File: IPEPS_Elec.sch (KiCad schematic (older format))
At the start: 6 parts

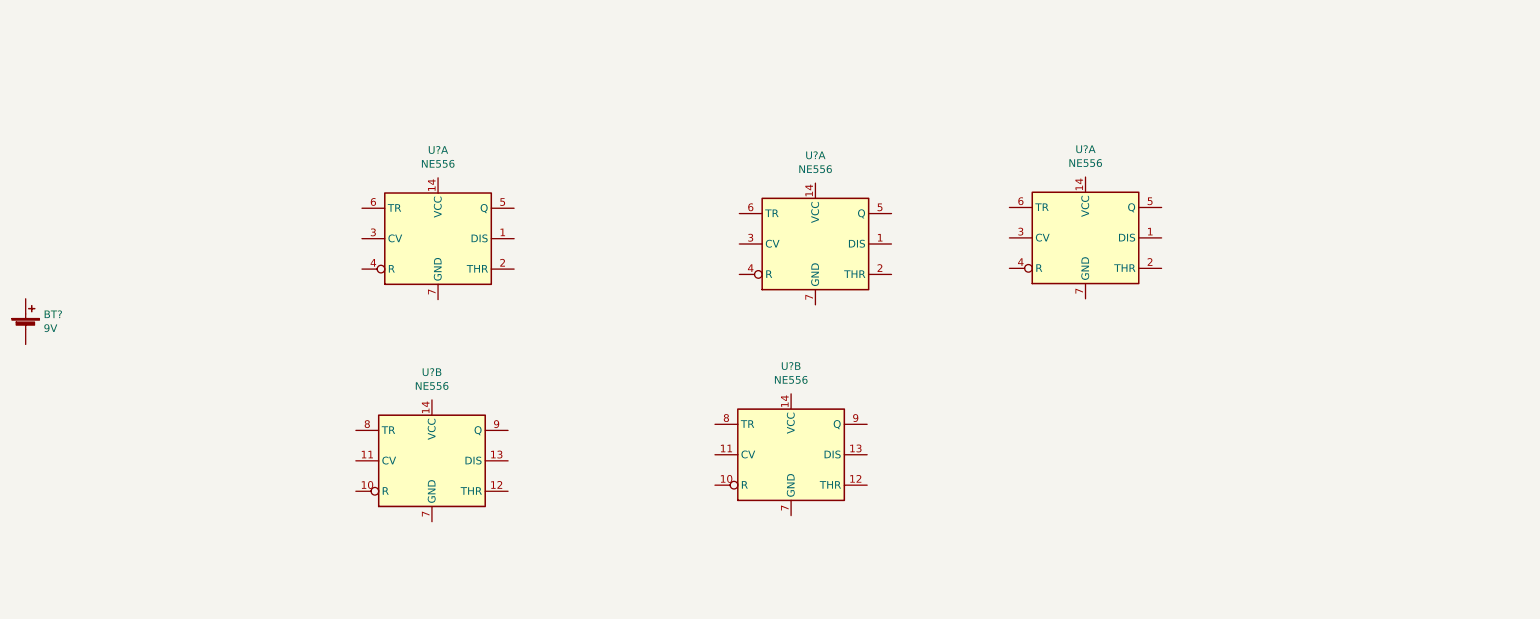
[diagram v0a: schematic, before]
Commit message: wire up the bistable 555 timers
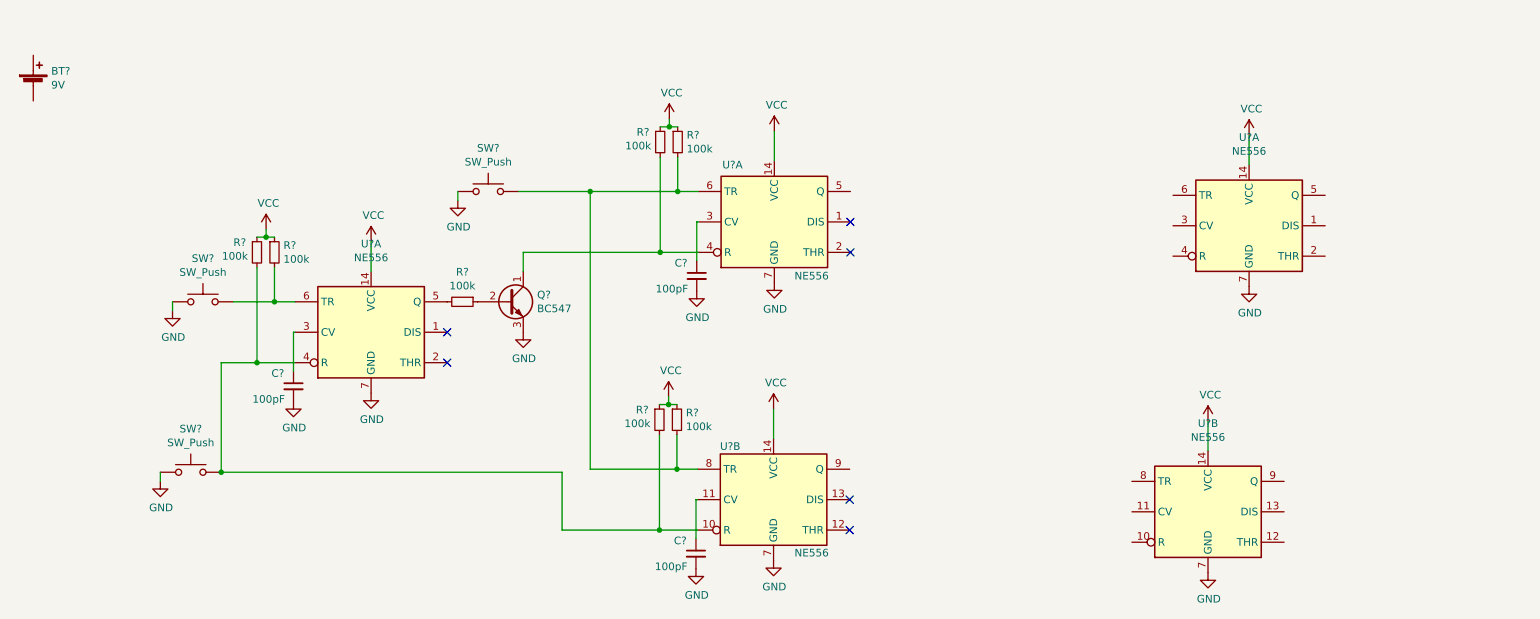
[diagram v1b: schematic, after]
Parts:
- added C? (x3): 100pF, symbol Device:C_Small
- added Q?: BC547, Package_TO_SOT_THT:TO-92_Inline, symbol Transistor_BJT:BC547
- added R? (x7): 100k, symbol Device:R_Small
- added SW? (x3): SW_Push, symbol Switch:SW_Push
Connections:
- net VCC: now reaches U?.14 (VCC)
- net VCC: now also U?.14 (VCC), U?.14 (VCC), U?.14 (VCC), U?.14 (VCC), R?.1, R?.1, R?.1, R?.1, R?.1, R?.1
- net at U?.3 (CV): now also C?.1 (x2)
- net at U?.4 (R): now also Q?.1 (C), R?.2
- net at U?.6 (TR): now also U?.8 (TR), R?.2, R?.2, SW?.2
- net GND: now reaches U?.7 (GND)
- net GND: now also U?.7 (GND), U?.7 (GND), U?.7 (GND), U?.7 (GND), C?.2, C?.2, C?.2, Q?.3 (E), SW?.1, SW?.1, SW?.1
- net at U?.10 (R): now also U?.4 (R), R?.2, R?.2, SW?.2
- net at U?.11 (CV): now also C?.1
- net at U?.5 (Q): now also R?.2
- net at U?.6 (TR): now also R?.2, SW?.2
- new net: Q?.2 (B), R?.1
- no-connect marks 0 -> 6
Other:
- moved on the sheet: BT?, U?A, U?B

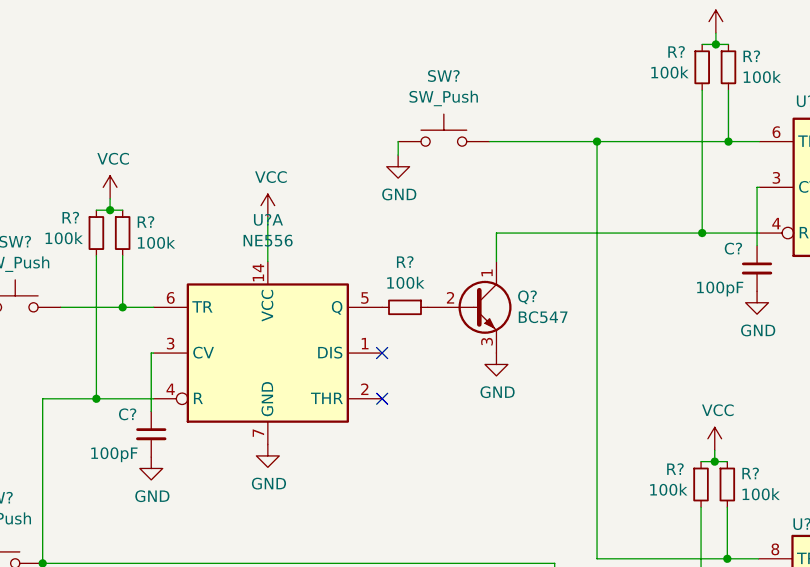
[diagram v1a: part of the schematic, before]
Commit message: fix transistor base value
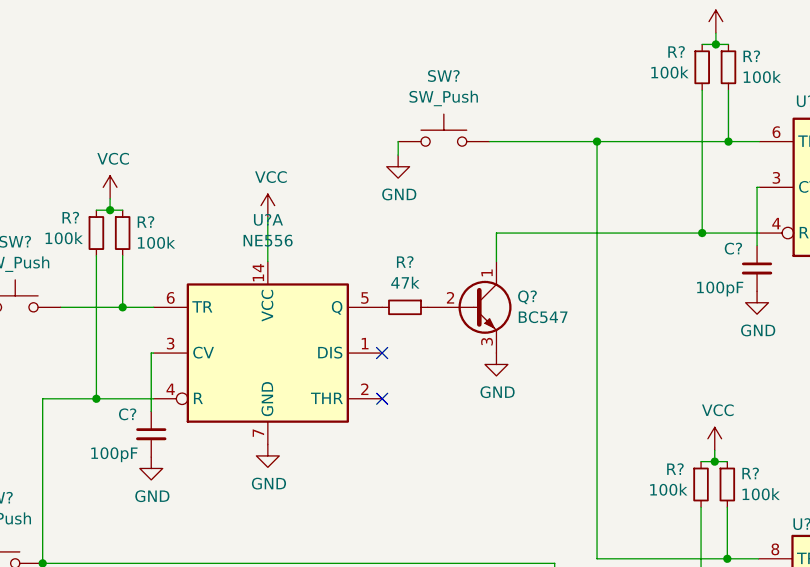
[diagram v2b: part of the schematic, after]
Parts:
- R?: value 100k -> 47k
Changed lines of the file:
@@
 P 3910 2585
 F 0 "R?" V 3714 2585 50  0000 C CNN
-F 1 "100k" V 3805 2585 50  0000 C CNN
+F 1 "47k" V 3805 2585 50  0000 C CNN
 F 2 "" H 3910 2585 50  0001 C CNN
 F 3 "~" H 3910 2585 50  0001 C CNN

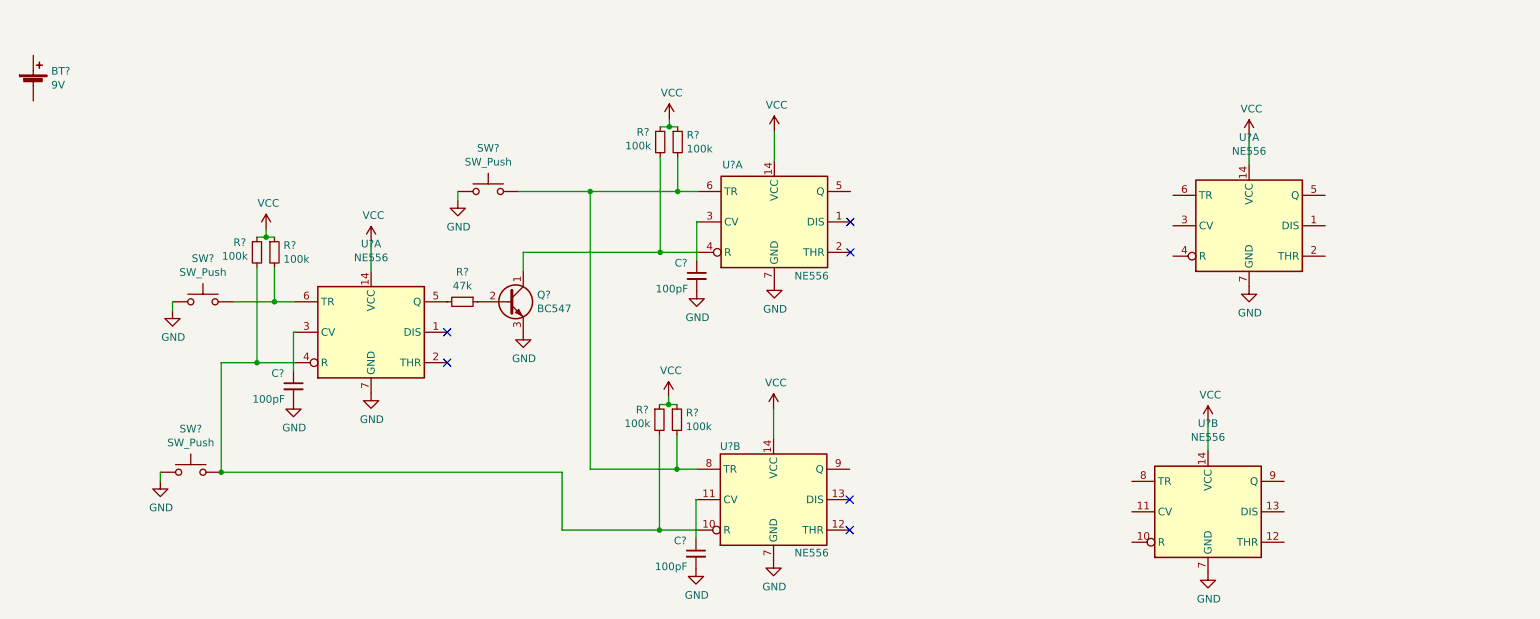
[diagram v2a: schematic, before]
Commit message: wire up monostable 555 timer
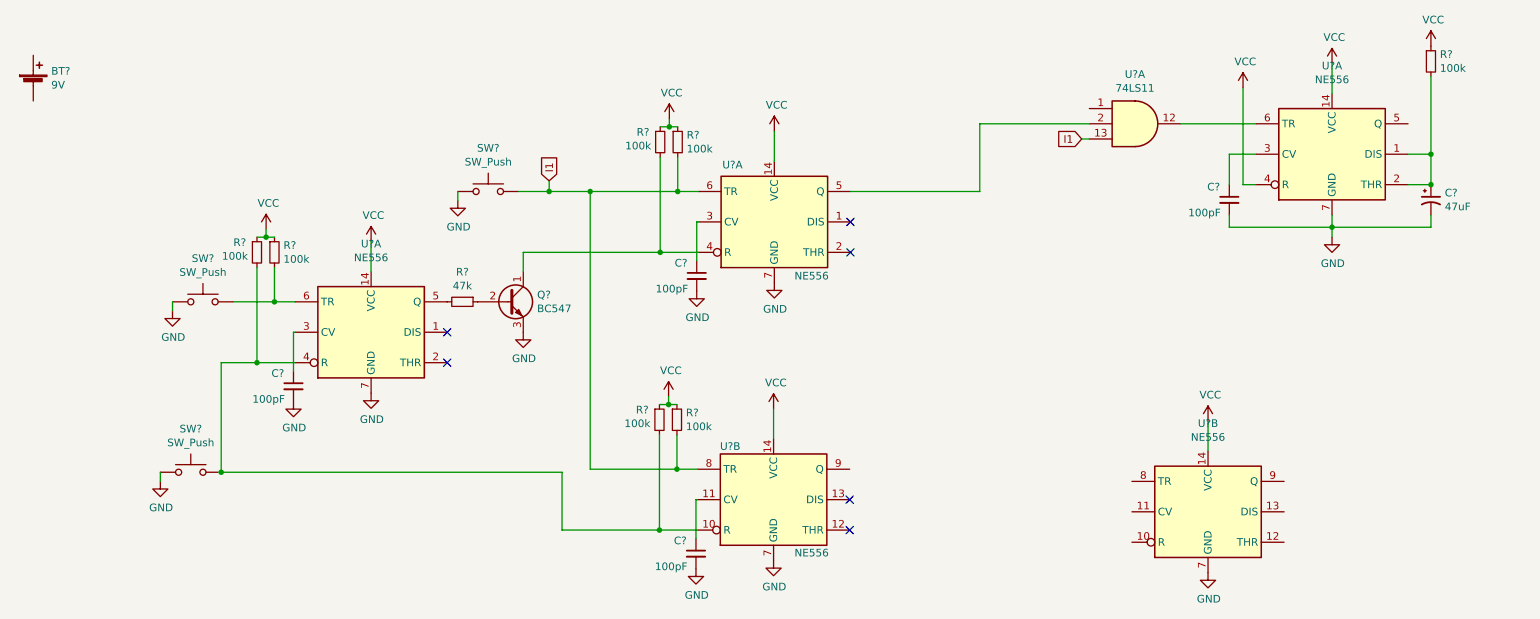
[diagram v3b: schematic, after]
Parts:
- added C?: 47uF, symbol Device:CP1_Small
- added C?: 100pF, symbol Device:C_Small
- added R?: 100k, symbol Device:R_Small
- added U?: 74LS11, symbol 74xx:74LS11
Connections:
- net GND: now also C?.2, C?.2
- net VCC: now also U?.4 (R), R?.1
- net at U?.5 (Q): now also U?.2
- net I1: now reaches R?.2, R?.2, SW?.2, U?.6 (TR), U?.8 (TR)
- net I1: now also U?.13
- net at U?.1 (DIS): now also U?.2 (THR), C?.1, R?.2
- net at U?.3 (CV): now also C?.1
- net at U?.6 (TR): now also U?.12
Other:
- moved on the sheet: U?A
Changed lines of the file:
@@
 L Timer:NE556 U?
 U 1 1 61904F77
-P 9080 2085
-F 0 "U?" H 9080 2666 50  0000 C CNN
-F 1 "NE556" H 9080 2575 50  0000 C CNN
-F 2 "" H 9080 2085 50  0001 C CNN
-F 3 "http://www.ti.com/lit/ds/symlink/ne556.pdf" H 9080 2085 50  0001 C CNN
-	1    9080 2085
+P 9625 1615
+F 0 "U?" H 9625 2196 50  0000 C CNN
+F 1 "NE556" H 9625 2105 50  0000 C CNN
+F 2 "" H 9625 1615 50  0001 C CNN
+F 3 "http://www.ti.com/lit/ds/symlink/ne556.pdf" H 9625 1615 50  0001 C CNN
+	1    9625 1615
 	1    0    0    -1
 $EndComp
@@
 L power:VCC #PWR?
 U 1 1 61936BE9
-P 9080 1490
-F 0 "#PWR?" H 9080 1340 50  0001 C CNN
-F 1 "VCC" H 9095 1663 50  0000 C CNN
-F 2 "" H 9080 1490 50  0001 C CNN
-F 3 "" H 9080 1490 50  0001 C CNN
-	1    9080 1490
-	1    0    0    -1
-$EndComp
-Wire Wire Line
-	9080 1685 9080 1490
+P 9625 1020
+F 0 "#PWR?" H 9625 870 50  0001 C CNN
+F 1 "VCC" H 9640 1193 50  0000 C CNN
+F 2 "" H 9625 1020 50  0001 C CNN
+F 3 "" H 9625 1020 50  0001 C CNN
+	1    9625 1020
+	1    0    0    -1
+$EndComp
+Wire Wire Line
+	9625 1215 9625 1020
 $Comp
 L power:VCC #PWR?
@@
 L power:GND #PWR?
 U 1 1 6193C618
-P 9080 2485
-F 0 "#PWR?" H 9080 2235 50  0001 C CNN
-F 1 "GND" H 9085 2312 50  0000 C CNN
-F 2 "" H 9080 2485 50  0001 C CNN
-F 3 "" H 9080 2485 50  0001 C CNN
-	1    9080 2485
+P 9625 2160
+F 0 "#PWR?" H 9625 1910 50  0001 C CNN
+F 1 "GND" H 9630 1987 50  0000 C CNN
+F 2 "" H 9625 2160 50  0001 C CNN
+F 3 "" H 9625 2160 50  0001 C CNN
+	1    9625 2160
 	1    0    0    -1
 $EndComp
@@
 	4750 3685 5320 3685
 Wire Wire Line
-	4280 1860 4750 1860
+	4280 1860 4480 1860
 Wire Wire Line
 	4750 1860 4750 3685
@@
 Wire Wire Line
 	1925 3705 1925 3765
+$Comp
+L Device:R_Small R?
+U 1 1 619EB70F
+P 10275 1005
+F 0 "R?" H 10334 1051 50  0000 L CNN
+F 1 "100k" H 10334 960 50  0000 L CNN
+F 2 "" H 10275 1005 50  0001 C CNN
+F 3 "~" H 10275 1005 50  0001 C CNN
+	1    10275 1005
+	1    0    0    -1
+$EndComp
+$Comp
+L power:VCC #PWR?
+U 1 1 619EC41F
+P 10275 905
+F 0 "#PWR?" H 10275 755 50  0001 C CNN
+F 1 "VCC" H 10290 1078 50  0000 C CNN
+F 2 "" H 10275 905 50  0001 C CNN
+F 3 "" H 10275 905 50  0001 C CNN
+	1    10275 905
+	1    0    0    -1
+$EndComp
+Wire Wire Line
+	10125 1615 10275 1615
+Wire Wire Line
+	10275 1105 10275 1615
+Wire Wire Line
+	10125 1815 10275 1815
+Wire Wire Line
+	10275 1815 10275 1615
+Connection ~ 10275 1615
+$Comp
+L Device:CP1_Small C?
+U 1 1 619F6519
+P 10275 1915
+F 0 "C?" H 10366 1961 50  0000 L CNN
+F 1 "47uF" H 10366 1870 50  0000 L CNN
+F 2 "" H 10275 1915 50  0001 C CNN
+F 3 "~" H 10275 1915 50  0001 C CNN
+	1    10275 1915
+	1    0    0    -1
+$EndComp
+Connection ~ 10275 1815
+$Comp
+L Device:C_Small C?
+U 1 1 619FB1EC
+P 8950 1915
+F 0 "C?" H 8805 2000 50  0000 L CNN
+F 1 "100pF" H 8680 1830 50  0000 L CNN
+F 2 "" H 8950 1915 50  0001 C CNN
+F 3 "~" H 8950 1915 50  0001 C CNN
+	1    8950 1915
+	1    0    0    -1
+$EndComp
+Wire Wire Line
+	9625 2015 9625 2095
+Wire Wire Line
+	10275 2015 10275 2095
+Wire Wire Line
+	10275 2095 9625 2095
+Connection ~ 9625 2095
+Wire Wire Line
+	9625 2095 9625 2160
+Wire Wire Line
+	8950 2015 8950 2095
+Wire Wire Line
+	8950 2095 9625 2095
+Wire Wire Line
+	9125 1615 8950 1615
+Wire Wire Line
+	8950 1615 8950 1815
+Wire Wire Line
+	9125 1815 9040 1815
+Wire Wire Line
+	9040 1815 9040 1180
+$Comp
+L power:VCC #PWR?
+U 1 1 61A07F28
+P 9040 1180
+F 0 "#PWR?" H 9040 1030 50  0001 C CNN
+F 1 "VCC" H 9055 1353 50  0000 C CNN
+F 2 "" H 9040 1180 50  0001 C CNN
+F 3 "" H 9040 1180 50  0001 C CNN
+	1    9040 1180
+	1    0    0    -1
+$EndComp
+$Comp
+L 74xx:74LS11 U?
+U 1 1 61A0CAE6
+P 8330 1415
+F 0 "U?" H 8330 1740 50  0000 C CNN
+F 1 "74LS11" H 8330 1649 50  0000 C CNN
+F 2 "" H 8330 1415 50  0001 C CNN
+F 3 "http://www.ti.com/lit/gpn/sn74LS11" H 8330 1415 50  0001 C CNN
+	1    8330 1415
+	1    0    0    -1
+$EndComp
+Wire Wire Line
+	9125 1415 8630 1415
+Text GLabel 4480 1790 1    50   Input ~ 0
+I1
+Wire Wire Line
+	4480 1790 4480 1860
+Connection ~ 4480 1860
+Wire Wire Line
+	4480 1860 4750 1860
+Text GLabel 7980 1515 0    50   Input ~ 0
+I1
+Wire Wire Line
+	8030 1515 7980 1515
+Wire Wire Line
+	6460 1860 7310 1860
+Wire Wire Line
+	7310 1860 7310 1415
+Wire Wire Line
+	7310 1415 8030 1415
 $EndSCHEMATC

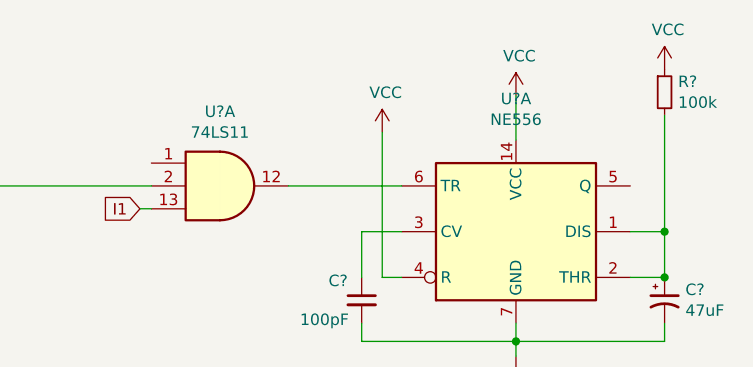
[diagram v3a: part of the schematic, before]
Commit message: add pull-up resistor to monostable reset pin
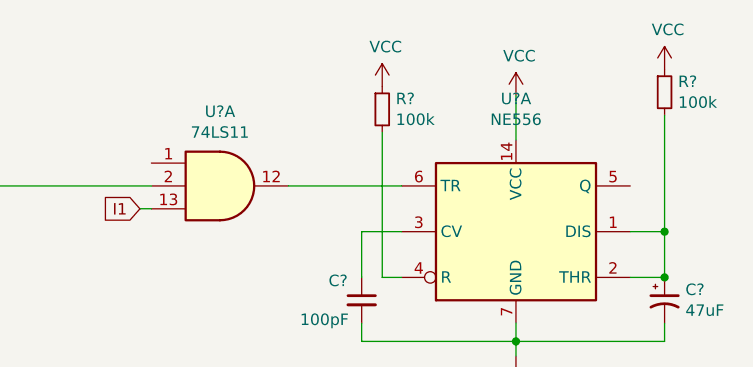
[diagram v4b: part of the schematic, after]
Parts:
- added R?: 100k, symbol Device:R_Small
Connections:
- net VCC: now also R?.1; no longer U?.4 (R)
- new net: R?.2, U?.4 (R)
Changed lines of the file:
@@
 L power:VCC #PWR?
 U 1 1 61A07F28
-P 9040 1180
-F 0 "#PWR?" H 9040 1030 50  0001 C CNN
-F 1 "VCC" H 9055 1353 50  0000 C CNN
-F 2 "" H 9040 1180 50  0001 C CNN
-F 3 "" H 9040 1180 50  0001 C CNN
-	1    9040 1180
+P 9040 980
+F 0 "#PWR?" H 9040 830 50  0001 C CNN
+F 1 "VCC" H 9055 1153 50  0000 C CNN
+F 2 "" H 9040 980 50  0001 C CNN
+F 3 "" H 9040 980 50  0001 C CNN
+	1    9040 980
 	1    0    0    -1
 $EndComp
@@
 Wire Wire Line
 	7310 1415 8030 1415
+$Comp
+L Device:R_Small R?
+U 1 1 61A2A7B2
+P 9040 1080
+F 0 "R?" H 9099 1126 50  0000 L CNN
+F 1 "100k" H 9099 1035 50  0000 L CNN
+F 2 "" H 9040 1080 50  0001 C CNN
+F 3 "~" H 9040 1080 50  0001 C CNN
+	1    9040 1080
+	1    0    0    -1
+$EndComp
 $EndSCHEMATC
